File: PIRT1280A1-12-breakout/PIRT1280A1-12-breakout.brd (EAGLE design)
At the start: 76.2 x 68.6 mm, 12 parts, among them U1 PIRT1280A1-12

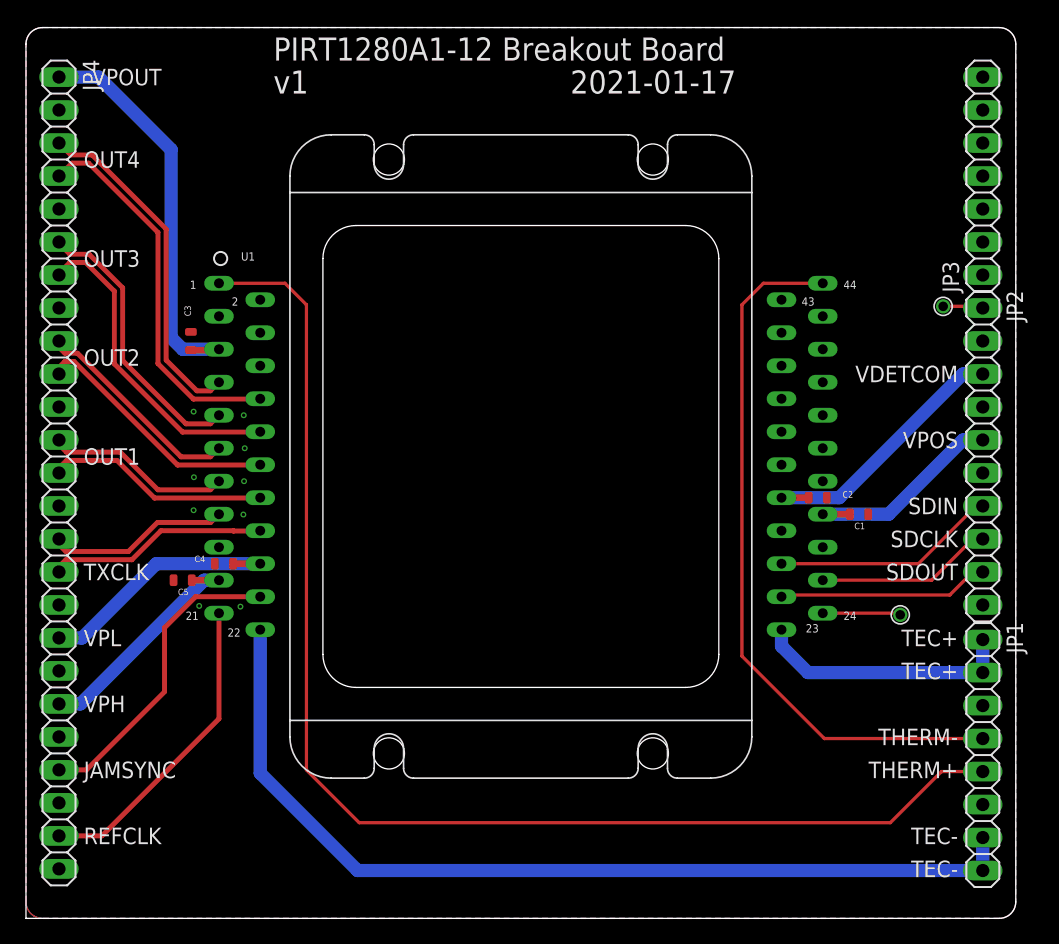
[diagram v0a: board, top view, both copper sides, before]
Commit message: Mods from Oliver and Scott; more testpoints, stitching, ground points.
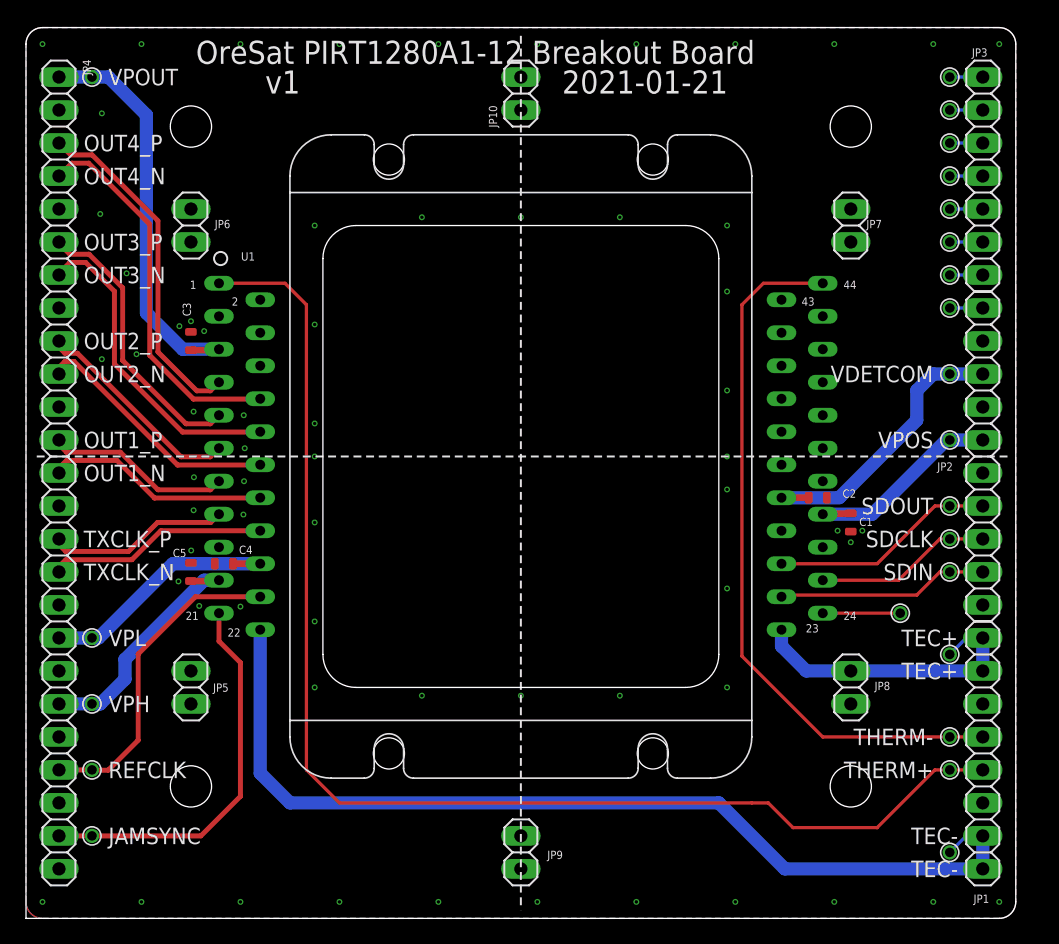
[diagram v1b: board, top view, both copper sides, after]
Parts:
- added JP10, JP5, JP6, JP7, JP8, JP9: (no value), pinhead:1X02
- added TP10, TP11, TP12, TP13, TP14, TP15, TP16, TP17, TP18, TP19, TP20, TP21, TP22, TP23, TP3, TP4, TP5, TP6, TP7, TP8, TP9: TEST-POINT-LARGE-SQUARE, oresat-misc:1X01
- moved C1 0.90 mm to (63.5, 30.5), turned to 270 degrees
- moved C5 0.90 mm to (12.7, 26.7), turned to 90 degrees
- moved TP2 0.52 mm to (71.1, 47.0)
- moved TP1 0.13 mm to (67.3, 23.5)
- moved JP1 0.13 mm to (73.7, 12.7)
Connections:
- net N$11 renamed ABITOUT
- new net N$2: JP3.7, TP9.1
- new net N$3: JP3.6, TP8.1
- new net N$4: JP3.5, TP7.1
- new net N$5: JP3.4, TP6.1
- new net N$6: JP3.3, TP5.1
- new net N$7: JP3.2, TP4.1
- new net N$8: JP3.1, TP3.1
- net GND: now also JP10.1, JP10.2, JP5.1, JP5.2, JP6.1, JP6.2, JP7.1, JP7.2, JP8.1, JP8.2, JP9.1, JP9.2
- net JAMSYNC: now also JP4.24, TP19.1, U1.21; no longer JP4.22, U1.20
- net REFCLK: now also JP4.22, TP20.1, U1.20; no longer JP4.24, U1.21
- net SDCLK: now also TP10.1
- net SDIN: now also JP2.9, TP11.1, U1.25; no longer JP2.7, U1.27
- net SDOUT: now also JP2.7, TP12.1, U1.27; no longer JP2.9, U1.25
- net TEC+: now also TP14.1
- net TEC-: now also TP13.1
- net THERM+: now also TP15.1
- net THERM-: now also TP16.1
- net VEDETCOM-2.9V: now also TP17.1
- net VPH-3.3V: now also TP21.1
- net VPL-1.6V: now also TP22.1
- net VPOS-3.3V: now also TP18.1
- net VPOUT-0.9V: now also TP23.1
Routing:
- net JAMSYNC: track 23.9 -> 30.0 mm
- net TEC-: track 72.3 -> 75.3 mm
- net TEC+: track 20.1 -> 23.2 mm
- net N$8: track 0.00 -> 2.54 mm
- net N$7: track 0.00 -> 2.54 mm
- net N$6: track 0.00 -> 2.54 mm
- net N$5: track 0.00 -> 2.54 mm
- net N$4: track 0.00 -> 2.54 mm
- net N$3: track 0.00 -> 2.54 mm
- net N$2: track 0.00 -> 2.54 mm
- net VEDETCOM-2.9V: track 21.6 -> 23.5 mm
- net SDIN: track 17.3 -> 16.3 mm
- net SDOUT: track 16.3 -> 17.3 mm
- net VPH-3.3V: track 18.4 -> 19.3 mm
- net REFCLK: track 24.2 -> 24.9 mm
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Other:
- board text added: "2021-01-21"
- board text added: "OUT1_N"
- board text added: "OUT1_P"
- board text added: "OUT2_N"
- board text added: "OUT2_P"
- board text added: "OUT3_N"
- board text added: "OUT3_P"
- board text added: "OUT4_N"
- board text added: "OUT4_P"
- board text added: "OreSat PIRT1280A1-12 Breakout Board"
- board text added: "TXCLK_N"
- board text added: "TXCLK_P"
- board text removed: "2021-01-17"
- board text removed: "OUT1"
- board text removed: "OUT2"
- board text removed: "OUT3"
- board text removed: "OUT4"
- board text removed: "PIRT1280A1-12 Breakout Board"
- board text removed: "TXCLK"
